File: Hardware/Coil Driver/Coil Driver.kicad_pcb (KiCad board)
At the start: 4 copper layers, 50 x 50 mm, 87 parts, among them J1 Barrel_Jack_Switch, J2 0.1" Header, J3 Tag-connect-NL, J4 0.1" Header, Q1 DMN3023L, Q2 DMN3023L, Q3 DMN3023L, Q4 DMN3023L, SW1 BTN_RST, SW2 BTN_USR1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

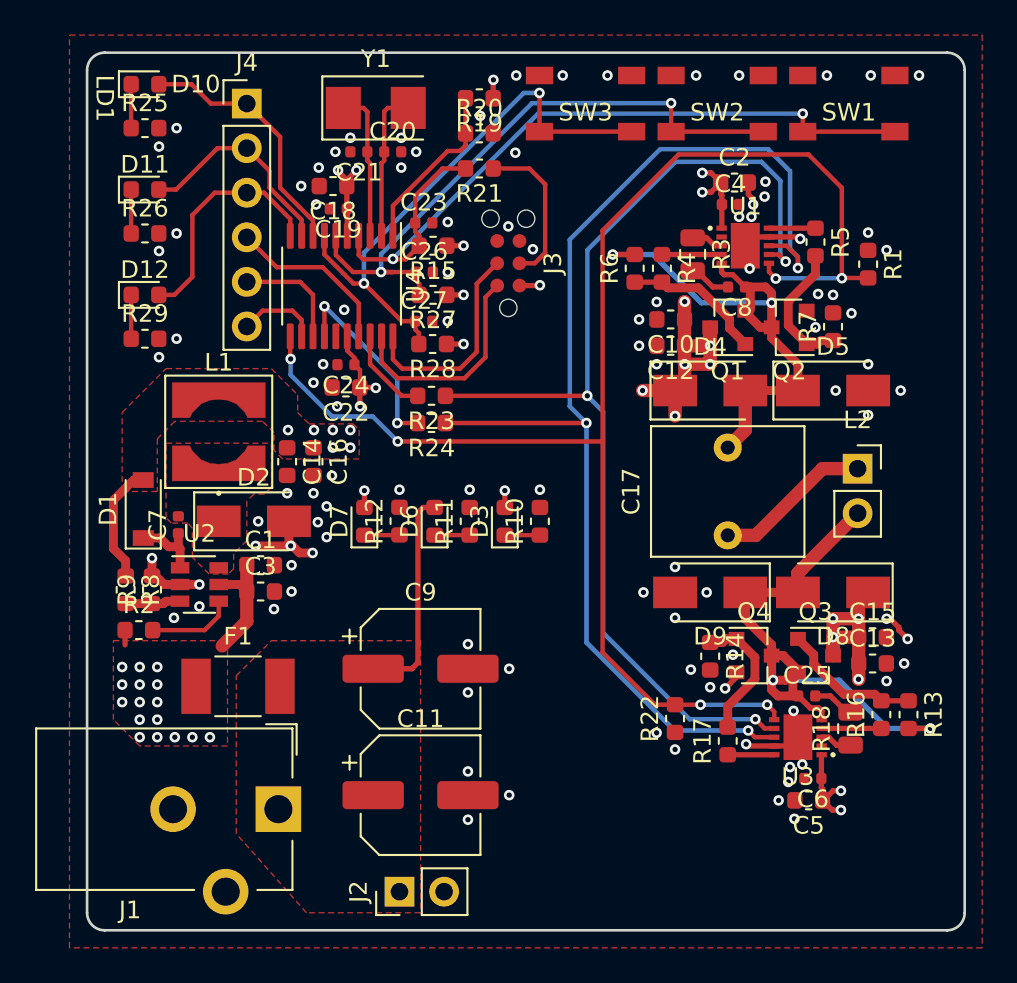
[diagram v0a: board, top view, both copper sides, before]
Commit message: Positioned all designators and added logo library
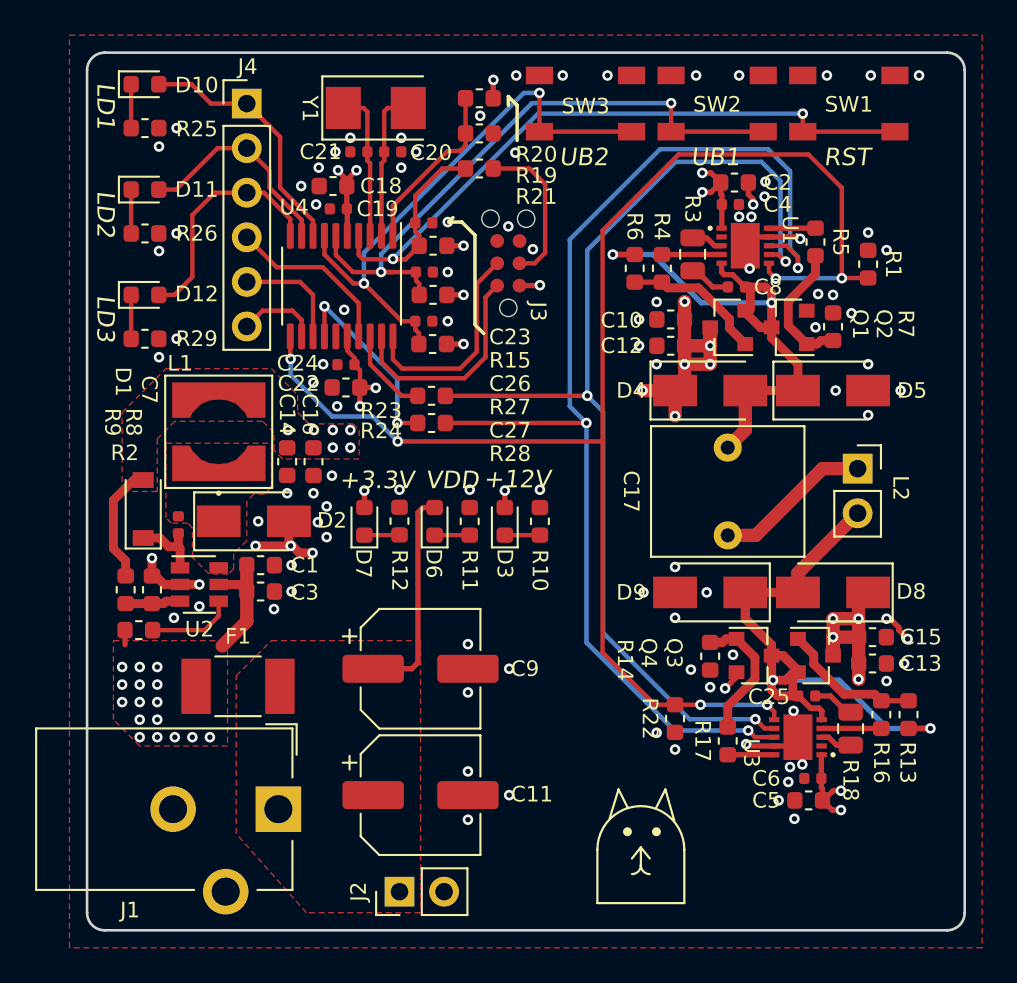
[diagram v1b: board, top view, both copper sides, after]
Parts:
- added REF**: ANDREW_CAT, LOGOS:ANDREW_CAT, F.Cu at (157.6, 121.5)
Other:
- board text added: "+12V"
- board text added: "+3.3V"
- board text added: "LD2"
- board text added: "LD3"
- board text added: "RST"
- board text added: "UB1"
- board text added: "UB2"
- board text added: "VDD"

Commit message: added ground stitching vias throughout board, and via fence around switching region. More or less ready to go.
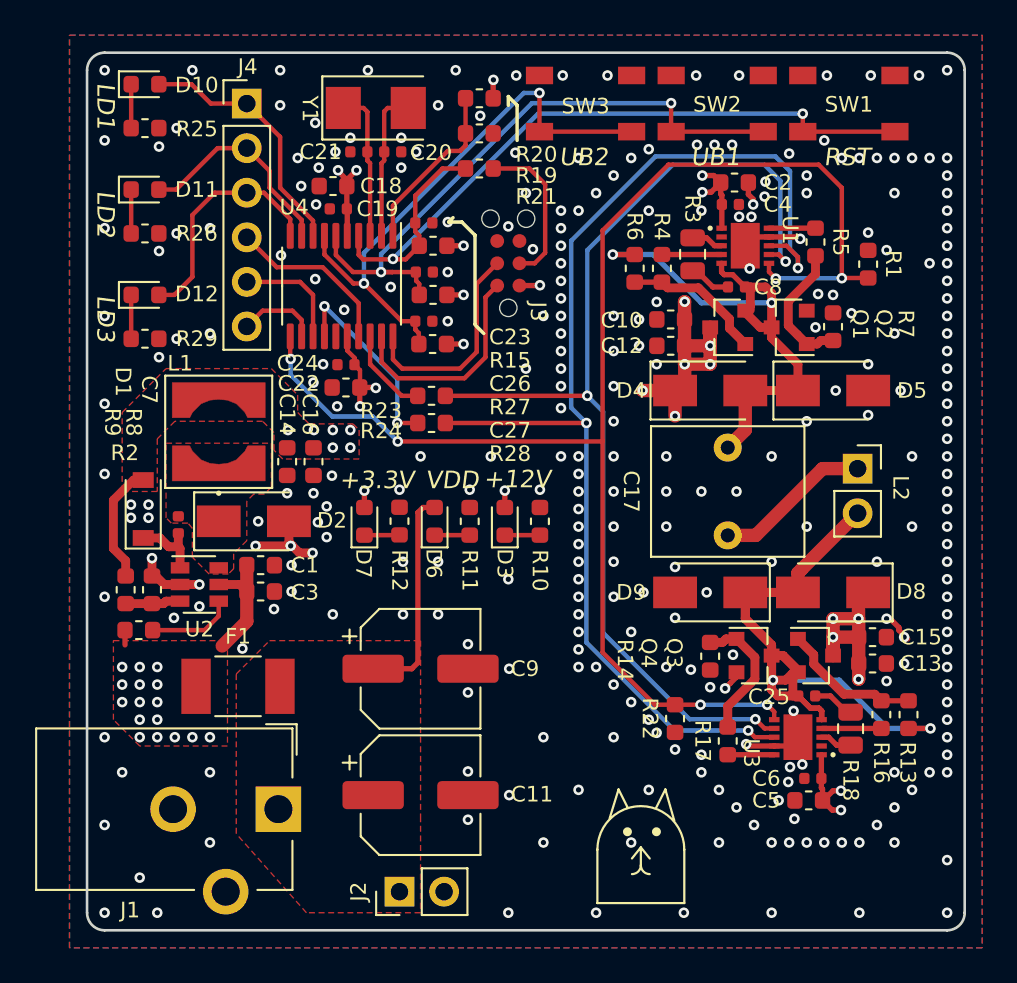
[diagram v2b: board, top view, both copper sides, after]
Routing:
- net GND: vias 101 -> 289
- net (no net): vias 0 -> 1
- added copper zone on B.Cu, net GND

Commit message: fixed DRCs caused by new vias. oops.
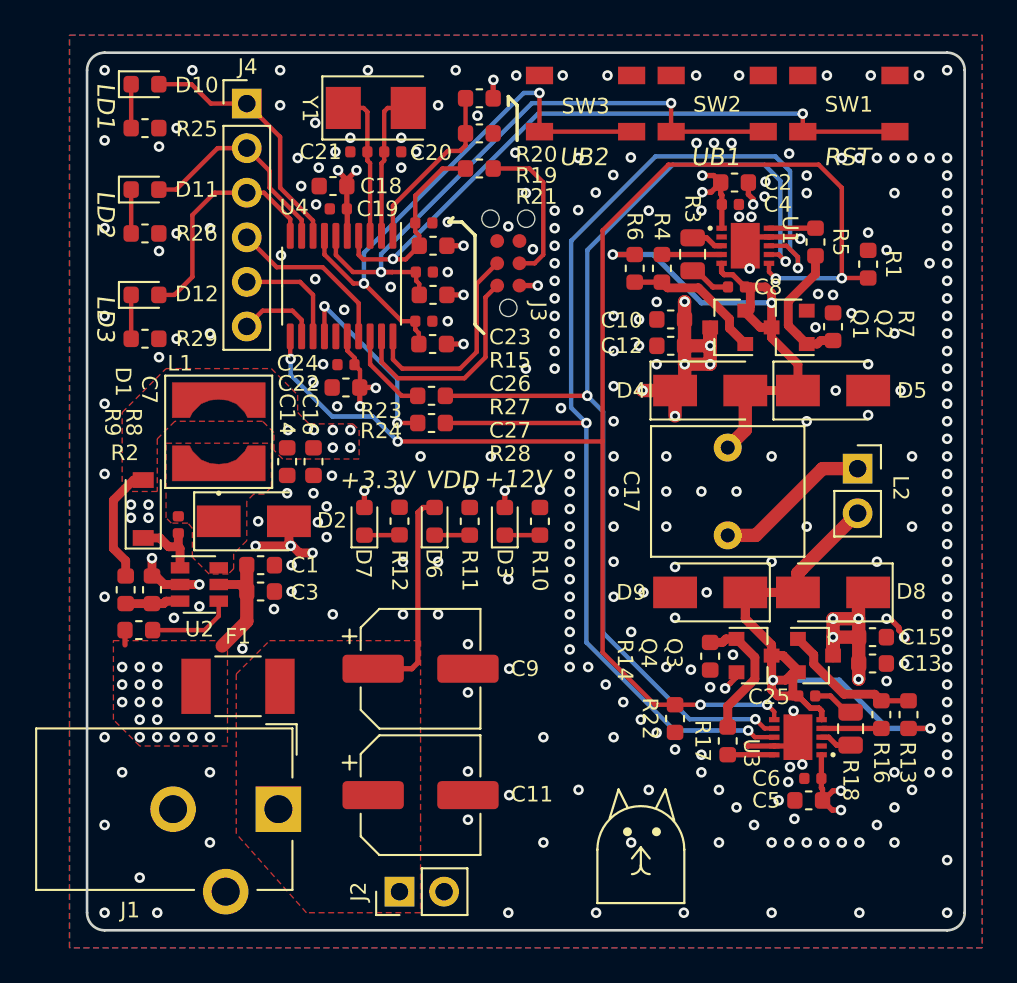
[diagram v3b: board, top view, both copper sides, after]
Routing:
- net GND: vias 289 -> 283
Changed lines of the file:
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@@
     (thickness 1.6)
     (drawings 25)
-    (tracks 789)
+    (tracks 782)
     (zones 0)
     (modules 88)
@@
   (segment (start 130.4 103.3) (end 131.3 103.3) (width 0.508) (layer F.Cu) (net 1))
   (segment (start 129.9125 102.8125) (end 130.4 103.3) (width 0.508) (layer F.Cu) (net 1))
-  (via (at 163.55 112.39519) (size 0.6) (drill 0.3) (layers F.Cu B.Cu) (net 1))
   (segment (start 163.65481 112.5) (end 163.55 112.39519) (width 0.3048) (layer F.Cu) (net 1))
   (segment (start 165.15 112.5) (end 163.65481 112.5) (width 0.3048) (layer F.Cu) (net 1))
@@
   (via (at 146.55 82.65) (size 0.6) (drill 0.3) (layers F.Cu B.Cu) (net 1))
   (via (at 150.4 78.7) (size 0.6) (drill 0.3) (layers F.Cu B.Cu) (net 1))
-  (via (at 148.4 76.6) (size 0.6) (drill 0.3) (layers F.Cu B.Cu) (net 1))
+  (via (at 148.24 76.59) (size 0.6) (drill 0.3) (layers F.Cu B.Cu) (net 1))
   (via (at 150.45 74.3) (size 0.6) (drill 0.3) (layers F.Cu B.Cu) (net 1))
   (via (at 153.1 74.3) (size 0.6) (drill 0.3) (layers F.Cu B.Cu) (net 1))
@@
   (via (at 151 81) (size 0.6) (drill 0.3) (layers F.Cu B.Cu) (net 1))
   (via (at 143.3 86.35) (size 0.6) (drill 0.3) (layers F.Cu B.Cu) (net 1))
-  (via (at 152 88) (size 0.6) (drill 0.3) (layers F.Cu B.Cu) (net 1))
-  (via (at 153 82) (size 0.6) (drill 0.3) (layers F.Cu B.Cu) (net 1))
+  (via (at 152.64 82) (size 0.6) (drill 0.3) (layers F.Cu B.Cu) (net 1))
   (via (at 144 105) (size 0.6) (drill 0.3) (layers F.Cu B.Cu) (net 1))
   (via (at 140 105) (size 0.6) (drill 0.3) (layers F.Cu B.Cu) (net 1))
@@
   (via (at 146 105) (size 0.6) (drill 0.3) (layers F.Cu B.Cu) (net 1))
   (via (at 146 102) (size 0.6) (drill 0.3) (layers F.Cu B.Cu) (net 1))
-  (via (at 154 102) (size 0.6) (drill 0.3) (layers F.Cu B.Cu) (net 1))
-  (via (at 154 105) (size 0.6) (drill 0.3) (layers F.Cu B.Cu) (net 1))
-  (via (at 154 96) (size 0.6) (drill 0.3) (layers F.Cu B.Cu) (net 1))
+  (via (at 153.5 102) (size 0.6) (drill 0.3) (layers F.Cu B.Cu) (net 1))
+  (via (at 153.5 105) (size 0.6) (drill 0.3) (layers F.Cu B.Cu) (net 1))
+  (via (at 153.5 96) (size 0.6) (drill 0.3) (layers F.Cu B.Cu) (net 1))
   (via (at 145 96) (size 0.6) (drill 0.3) (layers F.Cu B.Cu) (net 1))
   (via (at 149 96) (size 0.6) (drill 0.3) (layers F.Cu B.Cu) (net 1))
@@
   (via (at 171 102) (size 0.6) (drill 0.3) (layers F.Cu B.Cu) (net 1))
   (via (at 150 103) (size 0.6) (drill 0.3) (layers F.Cu B.Cu) (net 1))
-  (via (at 154 108) (size 0.6) (drill 0.3) (layers F.Cu B.Cu) (net 1))
+  (via (at 153.5 108) (size 0.6) (drill 0.3) (layers F.Cu B.Cu) (net 1))
   (via (at 154 115) (size 0.6) (drill 0.3) (layers F.Cu B.Cu) (net 1))
   (via (at 158 115) (size 0.6) (drill 0.3) (layers F.Cu B.Cu) (net 1))
-  (via (at 157 79) (size 0.6) (drill 0.3) (layers F.Cu B.Cu) (net 1))
-  (via (at 156 80) (size 0.6) (drill 0.3) (layers F.Cu B.Cu) (net 1))
-  (via (at 155 81) (size 0.6) (drill 0.3) (layers F.Cu B.Cu) (net 1))
-  (via (at 154 82) (size 0.6) (drill 0.3) (layers F.Cu B.Cu) (net 1))
-  (via (at 153 83) (size 0.6) (drill 0.3) (layers F.Cu B.Cu) (net 1))
-  (via (at 153 84) (size 0.6) (drill 0.3) (layers F.Cu B.Cu) (net 1))
-  (via (at 153 85) (size 0.6) (drill 0.3) (layers F.Cu B.Cu) (net 1))
-  (via (at 153 86) (size 0.6) (drill 0.3) (layers F.Cu B.Cu) (net 1))
-  (via (at 153 87) (size 0.6) (drill 0.3) (layers F.Cu B.Cu) (net 1))
-  (via (at 153 88) (size 0.6) (drill 0.3) (layers F.Cu B.Cu) (net 1))
-  (via (at 153 89) (size 0.6) (drill 0.3) (layers F.Cu B.Cu) (net 1))
-  (via (at 153 90) (size 0.6) (drill 0.3) (layers F.Cu B.Cu) (net 1))
-  (via (at 153 91) (size 0.6) (drill 0.3) (layers F.Cu B.Cu) (net 1))
-  (via (at 153 96) (size 0.6) (drill 0.3) (layers F.Cu B.Cu) (net 1))
-  (via (at 154 97) (size 0.6) (drill 0.3) (layers F.Cu B.Cu) (net 1))
-  (via (at 154 98) (size 0.6) (drill 0.3) (layers F.Cu B.Cu) (net 1))
-  (via (at 154 99) (size 0.6) (drill 0.3) (layers F.Cu B.Cu) (net 1))
-  (via (at 154 100) (size 0.6) (drill 0.3) (layers F.Cu B.Cu) (net 1))
-  (via (at 154 101) (size 0.6) (drill 0.3) (layers F.Cu B.Cu) (net 1))
-  (via (at 154 103) (size 0.6) (drill 0.3) (layers F.Cu B.Cu) (net 1))
-  (via (at 154 104) (size 0.6) (drill 0.3) (layers F.Cu B.Cu) (net 1))
-  (via (at 154 106) (size 0.6) (drill 0.3) (layers F.Cu B.Cu) (net 1))
-  (via (at 155 108) (size 0.6) (drill 0.3) (layers F.Cu B.Cu) (net 1))
-  (via (at 154 107) (size 0.6) (drill 0.3) (layers F.Cu B.Cu) (net 1))
-  (via (at 156 109) (size 0.6) (drill 0.3) (layers F.Cu B.Cu) (net 1))
-  (via (at 157 110) (size 0.6) (drill 0.3) (layers F.Cu B.Cu) (net 1))
-  (via (at 158 111) (size 0.6) (drill 0.3) (layers F.Cu B.Cu) (net 1))
+  (via (at 156.98 78.97) (size 0.6) (drill 0.3) (layers F.Cu B.Cu) (net 1))
+  (via (at 155.98 79.97) (size 0.6) (drill 0.3) (layers F.Cu B.Cu) (net 1))
+  (via (at 154.98 80.97) (size 0.6) (drill 0.3) (layers F.Cu B.Cu) (net 1))
+  (via (at 153.98 81.97) (size 0.6) (drill 0.3) (layers F.Cu B.Cu) (net 1))
+  (via (at 152.64 83) (size 0.6) (drill 0.3) (layers F.Cu B.Cu) (net 1))
+  (via (at 152.64 84) (size 0.6) (drill 0.3) (layers F.Cu B.Cu) (net 1))
+  (via (at 152.64 85) (size 0.6) (drill 0.3) (layers F.Cu B.Cu) (net 1))
+  (via (at 152.64 86) (size 0.6) (drill 0.3) (layers F.Cu B.Cu) (net 1))
+  (via (at 152.64 87) (size 0.6) (drill 0.3) (layers F.Cu B.Cu) (net 1))
+  (via (at 152.64 88) (size 0.6) (drill 0.3) (layers F.Cu B.Cu) (net 1))
+  (via (at 152.64 89) (size 0.6) (drill 0.3) (layers F.Cu B.Cu) (net 1))
+  (via (at 152.64 90) (size 0.6) (drill 0.3) (layers F.Cu B.Cu) (net 1))
+  (via (at 152.64 91) (size 0.6) (drill 0.3) (layers F.Cu B.Cu) (net 1))
+  (via (at 153.5 97) (size 0.6) (drill 0.3) (layers F.Cu B.Cu) (net 1))
+  (via (at 153.5 98) (size 0.6) (drill 0.3) (layers F.Cu B.Cu) (net 1))
+  (via (at 153.5 99) (size 0.6) (drill 0.3) (layers F.Cu B.Cu) (net 1))
+  (via (at 153.5 100) (size 0.6) (drill 0.3) (layers F.Cu B.Cu) (net 1))
+  (via (at 153.5 101) (size 0.6) (drill 0.3) (layers F.Cu B.Cu) (net 1))
+  (via (at 153.5 103) (size 0.6) (drill 0.3) (layers F.Cu B.Cu) (net 1))
+  (via (at 153.5 104) (size 0.6) (drill 0.3) (layers F.Cu B.Cu) (net 1))
+  (via (at 153.5 106) (size 0.6) (drill 0.3) (layers F.Cu B.Cu) (net 1))
+  (via (at 154.55 108) (size 0.6) (drill 0.3) (layers F.Cu B.Cu) (net 1))
+  (via (at 153.5 107) (size 0.6) (drill 0.3) (layers F.Cu B.Cu) (net 1))
+  (via (at 155.55 109) (size 0.6) (drill 0.3) (layers F.Cu B.Cu) (net 1))
+  (via (at 156.55 110) (size 0.6) (drill 0.3) (layers F.Cu B.Cu) (net 1))
+  (via (at 157.55 111) (size 0.6) (drill 0.3) (layers F.Cu B.Cu) (net 1))
   (via (at 161 113) (size 0.6) (drill 0.3) (layers F.Cu B.Cu) (net 1))
   (via (at 161 114) (size 0.6) (drill 0.3) (layers F.Cu B.Cu) (net 1))
@@
   (via (at 173 79) (size 0.6) (drill 0.3) (layers F.Cu B.Cu) (net 1))
   (via (at 174 79) (size 0.6) (drill 0.3) (layers F.Cu B.Cu) (net 1))
-  (via (at 168 78) (size 0.6) (drill 0.3) (layers F.Cu B.Cu) (net 1))
-  (via (at 160.75 78.25) (size 0.6) (drill 0.3) (layers F.Cu B.Cu) (net 1))
-  (via (at 161.75 78.25) (size 0.6) (drill 0.3) (layers F.Cu B.Cu) (net 1))
-  (via (at 162.75 78.25) (size 0.6) (drill 0.3) (layers F.Cu B.Cu) (net 1))
-  (via (at 158 78.5) (size 0.6) (drill 0.3) (layers F.Cu B.Cu) (net 1))
-  (via (at 153 92) (size 0.6) (drill 0.3) (layers F.Cu B.Cu) (net 1))
+  (via (at 160.72 78.15) (size 0.6) (drill 0.3) (layers F.Cu B.Cu) (net 1))
+  (via (at 161.72 78.15) (size 0.6) (drill 0.3) (layers F.Cu B.Cu) (net 1))
+  (via (at 162.72 78.15) (size 0.6) (drill 0.3) (layers F.Cu B.Cu) (net 1))
   (via (at 153 93.25) (size 0.6) (drill 0.3) (layers F.Cu B.Cu) (net 1))
   (via (at 129.5 98.75) (size 0.6) (drill 0.3) (layers F.Cu B.Cu) (net 1))
@@
   (segment (start 149.1375 75.6) (end 149.1375 74.5625) (width 0.3048) (layer F.Cu) (net 7))
   (segment (start 149.1375 74.5625) (end 149.15 74.55) (width 0.3048) (layer F.Cu) (net 7))
-  (segment (start 150.635 86.27) (end 151.78 86.27) (width 0.3048) (layer F.Cu) (net 7))
-  (via (at 151.8 86.25) (size 0.6) (drill 0.3) (layers F.Cu B.Cu) (net 7))
-  (segment (start 151.78 86.27) (end 151.8 86.25) (width 0.3048) (layer F.Cu) (net 7))
   (via (at 141.8 97.95) (size 0.6) (drill 0.3) (layers F.Cu B.Cu) (net 7))
   (segment (start 141.8 98.9125) (end 141.8 97.95) (width 0.3048) (layer F.Cu) (net 7))
+  (via (at 151.68 86.27) (size 0.6) (drill 0.3) (layers F.Cu B.Cu) (net 7))
+  (segment (start 150.635 86.27) (end 151.68 86.27) (width 0.3048) (layer F.Cu) (net 7))
   (segment (start 144.7 83.2) (end 144.7 82.7) (width 0.254) (layer F.Cu) (net 8))
   (segment (start 144.925 84) (end 144.925 83.425) (width 0.254) (layer F.Cu) (net 8))
@@
   (segment (start 147.25 91) (end 148.2 90.05) (width 0.254) (layer F.Cu) (net 14))
   (segment (start 148.2 90.05) (end 148.2 86.165) (width 0.254) (layer F.Cu) (net 14))
-  (segment (start 149.1375 79.6) (end 151.2 79.6) (width 0.254) (layer F.Cu) (net 15))
-  (segment (start 151.2 79.6) (end 152.1 80.5) (width 0.254) (layer F.Cu) (net 15))
-  (segment (start 152.1 80.5) (end 152.1 84.4) (width 0.254) (layer F.Cu) (net 15))
   (segment (start 151.5 85) (end 150.635 85) (width 0.254) (layer F.Cu) (net 15))
-  (segment (start 152.1 84.4) (end 151.5 85) (width 0.254) (layer F.Cu) (net 15))
+  (segment (start 151.99 84.51) (end 151.5 85) (width 0.254) (layer F.Cu) (net 15))
+  (segment (start 151.99 80.39) (end 151.99 84.51) (width 0.254) (layer F.Cu) (net 15))
+  (segment (start 149.1375 79.6) (end 151.2 79.6) (width 0.254) (layer F.Cu) (net 15))
+  (segment (start 151.2 79.6) (end 151.99 80.39) (width 0.254) (layer F.Cu) (net 15))
   (segment (start 158.75 86.075) (end 157.2 86.075) (width 0.3048) (layer F.Cu) (net 16))
   (segment (start 162.6 88.168478) (end 162.6 88.7) (width 0.508) (layer F.Cu) (net 16))

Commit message: added silkscreen label and rev
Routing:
- net GND: vias 283 -> 281
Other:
- board text added: "01/2021"
- board text added: "A. Ge"
- board text added: "WPT Driver V1.0"

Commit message: Removed a bunch of ground vias (especially stitching around switching area) that were causing discontinuity in 12V pour in power layer
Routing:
- net GND: vias 281 -> 221
- net (no net): vias 1 -> 0
